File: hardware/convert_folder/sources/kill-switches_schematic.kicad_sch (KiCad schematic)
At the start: 6 parts, among them CN26 JST 2 position header 2.5mm, CN4 6 pin Picoblade, CN5 6 pin Picoblade, CN6 4 pin Picoblade, SW2 SW-T3-2B-A-A3-S1, SW3 SW-T3-2B-A-A3-S1

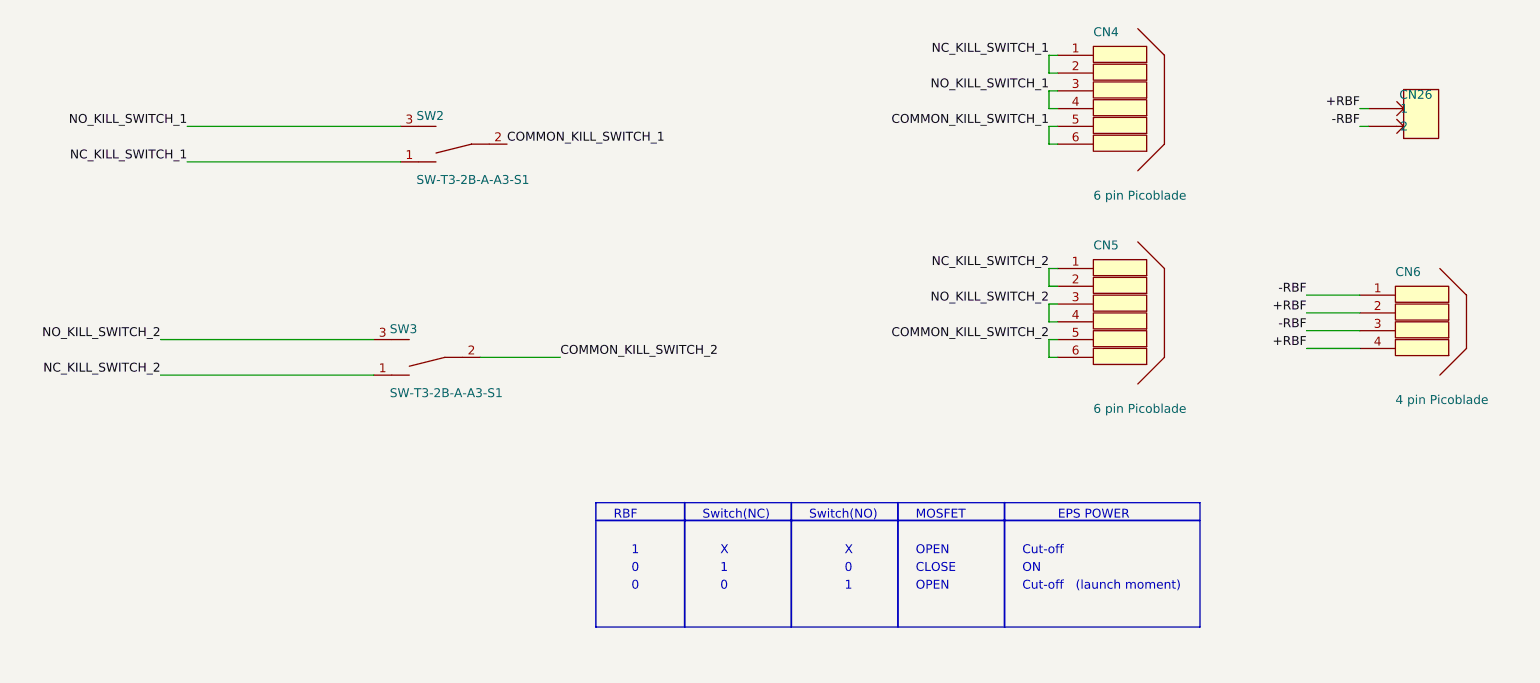
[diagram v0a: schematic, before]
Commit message: fix: fix a lot of connections between blocks. Many more to go...
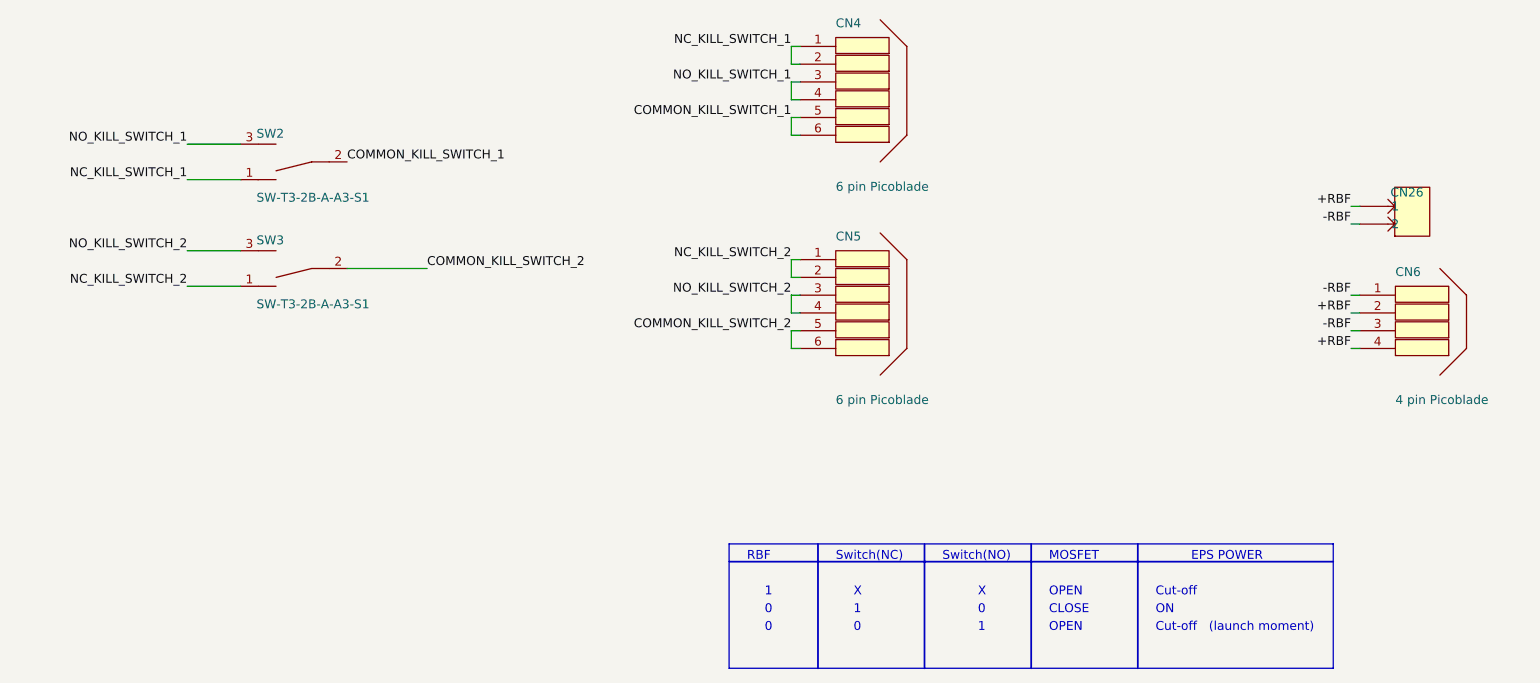
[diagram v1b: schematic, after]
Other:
- moved on the sheet: CN26, CN4, CN5, SW2, SW3

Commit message: fix: convert 90% of the schematic (there are 21 warnings/errors to resolve)
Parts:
- CN26: footprint B2B-XH-A-M(LF)(SN) -> altium_import:B2B-XH-A-M(LF)(SN); symbol flatsat_platform_2:root_0_B2B-XH-A-M(LF)(SN)_flatsat_platform_2.SchLib -> altium_import:root_0_B2B-XH-A-M(LF)(SN)_flatsat_platform_2.SchLib
- CN4, CN5: footprint PICO BLADE 0532610671 -> altium_import:PICO BLADE 0532610671; symbol flatsat_platform_2:root_0_mirrored_53398-0671_flatsat_platform_2.SchLib -> altium_import:root_0_mirrored_53398-0671_flatsat_platform_2.SchLib
- CN6: footprint PICO BLADE 0532610471 -> altium_import:PICO BLADE 0532610471; symbol flatsat_platform_2:root_0_mirrored_0533980471_flatsat_platform_2.SchLib -> altium_import:root_0_mirrored_0533980471_flatsat_platform_2.SchLib
- SW2, SW3: footprint SW-T3-2B-A-A3-S1 -> altium_import:SW-T3-2B-A-A3-S1; symbol SW-T3-2B-A-A3-S1:root_2_SW-T3-2B-A-A3-S1_SW-T3-2B-A-A3-S1.SchLib -> altium_import:root_2_SW-T3-2B-A-A3-S1_SW-T3-2B-A-A3-S1.SchLib
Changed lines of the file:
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@@
 	)
 	(symbol
-		(lib_id "flatsat_platform_2:root_0_mirrored_53398-0671_flatsat_platform_2.SchLib")
+		(lib_id "altium_import:root_0_mirrored_53398-0671_flatsat_platform_2.SchLib")
 		(at 166.37 77.47 270)
 		(mirror x)
@@
 			)
 		)
-		(property "Footprint" "PICO BLADE 0532610671"
+		(property "Footprint" "altium_import:PICO BLADE 0532610671"
 			(at 166.37 77.47 0)
 			(effects
@@
 	)
 	(symbol
-		(lib_id "flatsat_platform_2:root_0_B2B-XH-A-M(LF)(SN)_flatsat_platform_2.SchLib")
+		(lib_id "altium_import:root_0_B2B-XH-A-M(LF)(SN)_flatsat_platform_2.SchLib")
 		(at 228.6 92.71 90)
 		(unit 1)
@@
 			)
 		)
-		(property "Footprint" "B2B-XH-A-M(LF)(SN)"
+		(property "Footprint" "altium_import:B2B-XH-A-M(LF)(SN)"
 			(at 228.6 92.71 0)
 			(effects
@@
 	)
 	(symbol
-		(lib_id "flatsat_platform_2:root_0_mirrored_53398-0671_flatsat_platform_2.SchLib")
+		(lib_id "altium_import:root_0_mirrored_53398-0671_flatsat_platform_2.SchLib")
 		(at 166.37 107.95 270)
 		(mirror x)
@@
 			)
 		)
-		(property "Footprint" "PICO BLADE 0532610671"
+		(property "Footprint" "altium_import:PICO BLADE 0532610671"
 			(at 166.37 107.95 0)
 			(effects
@@
 	)
 	(symbol
-		(lib_id "SW-T3-2B-A-A3-S1:root_2_SW-T3-2B-A-A3-S1_SW-T3-2B-A-A3-S1.SchLib")
+		(lib_id "altium_import:root_2_SW-T3-2B-A-A3-S1_SW-T3-2B-A-A3-S1.SchLib")
 		(at 66.04 85.09 270)
 		(unit 1)
@@
 			)
 		)
-		(property "Footprint" "SW-T3-2B-A-A3-S1"
+		(property "Footprint" "altium_import:SW-T3-2B-A-A3-S1"
 			(at 66.04 85.09 0)
 			(effects
@@
 	)
 	(symbol
-		(lib_id "flatsat_platform_2:root_0_mirrored_0533980471_flatsat_platform_2.SchLib")
+		(lib_id "altium_import:root_0_mirrored_0533980471_flatsat_platform_2.SchLib")
 		(at 241.3 106.68 270)
 		(mirror x)
@@
 			)
 		)
-		(property "Footprint" "PICO BLADE 0532610471"
+		(property "Footprint" "altium_import:PICO BLADE 0532610471"
 			(at 241.3 106.68 0)
 			(effects
@@
 	)
 	(symbol
-		(lib_id "SW-T3-2B-A-A3-S1:root_2_SW-T3-2B-A-A3-S1_SW-T3-2B-A-A3-S1.SchLib")
+		(lib_id "altium_import:root_2_SW-T3-2B-A-A3-S1_SW-T3-2B-A-A3-S1.SchLib")
 		(at 66.04 100.33 270)
 		(unit 1)
@@
 			)
 		)
-		(property "Footprint" "SW-T3-2B-A-A3-S1"
+		(property "Footprint" "altium_import:SW-T3-2B-A-A3-S1"
 			(at 66.04 100.33 0)
 			(effects
